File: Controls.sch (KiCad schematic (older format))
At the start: 2 parts

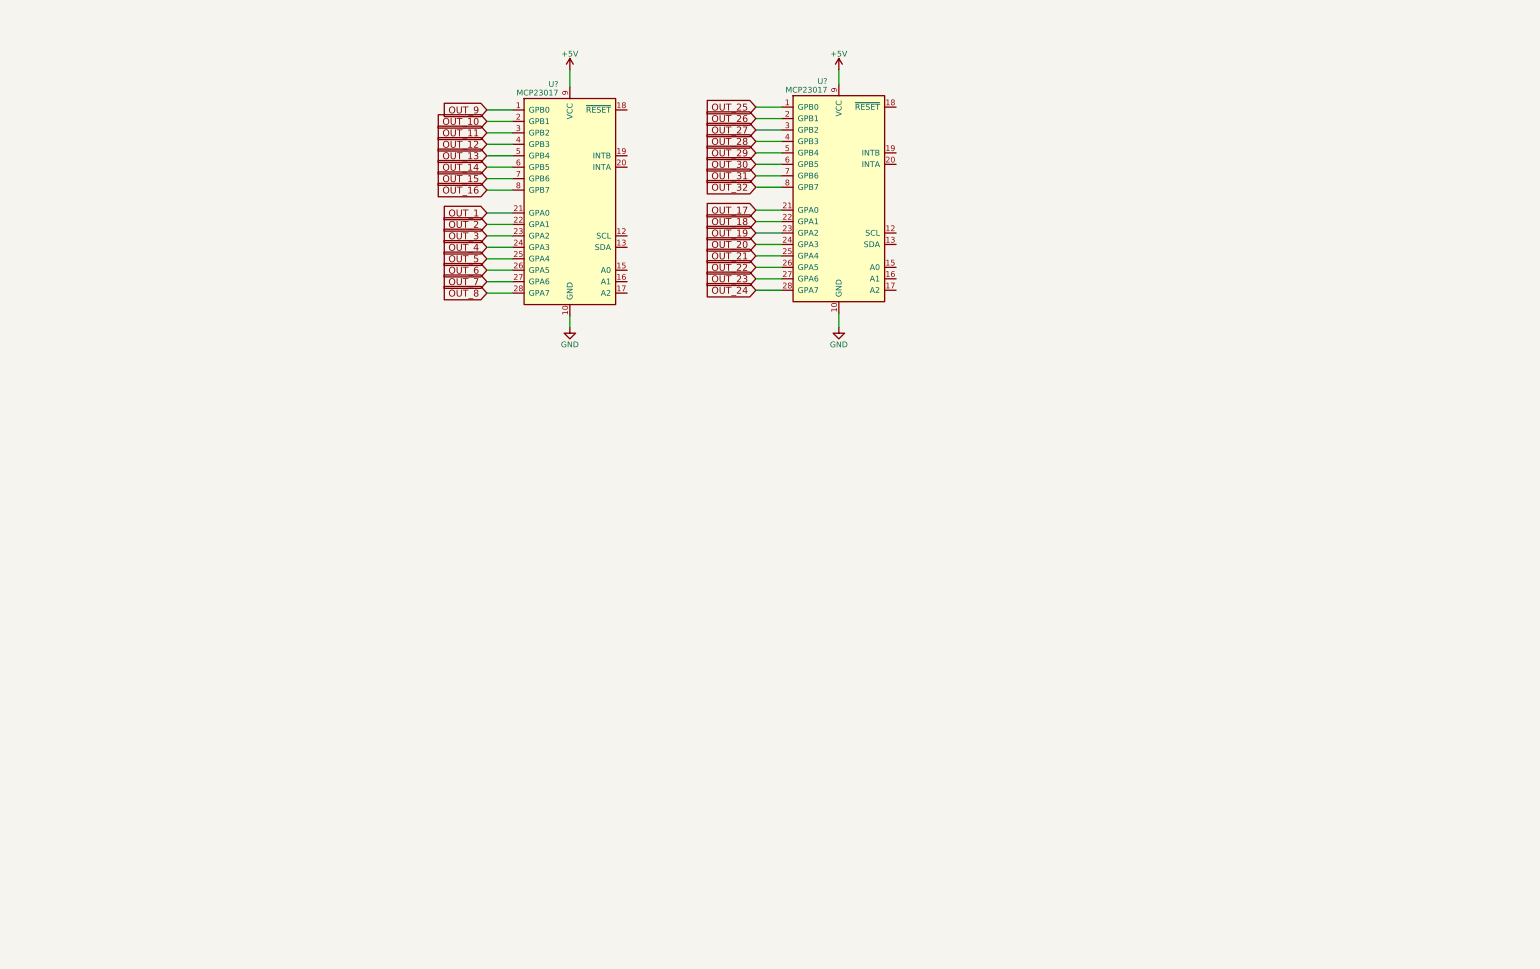
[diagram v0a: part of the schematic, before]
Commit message: Created arduino nano library for controls, no footprint yet. Created led-driver sheet for outputs from GPO to drive n-channel fets for low side driven control of led's
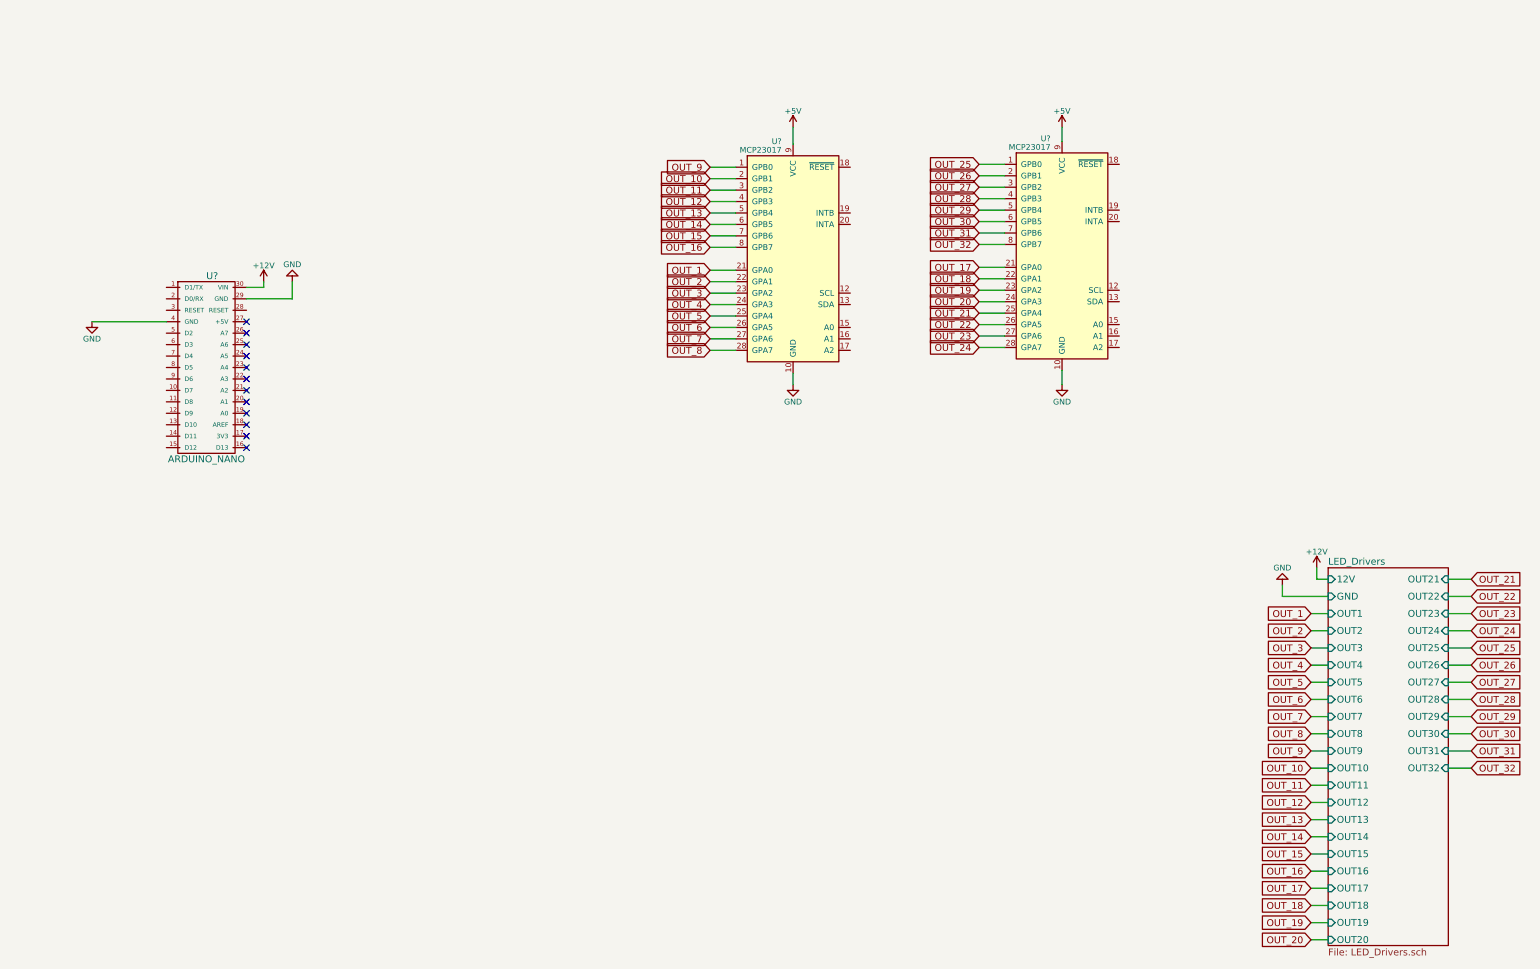
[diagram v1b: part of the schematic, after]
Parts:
- added U?: ARDUINO_NANO, symbol ARDUINO_NANO
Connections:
- net +12V: now also U?.30 (VIN)
- net GND: now also U?.29 (GND), U?.4 (GND)
- no-connect marks 0 -> 12
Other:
- moved on the sheet: U?

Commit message: Placed i2c labels and pull ups. Added 4 user input switches and MCP7940N RTC. Need to calculate capactiance for oscillator.
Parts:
- removed U? (x2): MCP23017, symbol MCP23017
- added BT?: Battery_Cell, symbol Battery_Cell
- added C? (x2): C, symbol C
- added R? (x7): 4.7K, symbol R
- added R?: 10K, symbol R
- added SW? (x4): SW_Push, symbol SW_Push
- added U? (x2): MCP23017, symbol MCP23017
- added U?: MCP7940N, symbol MCP7940N
- added Y?: Crystal, symbol Crystal
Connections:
- net labels added: MFP, SCL, SDA
- wire segments 83 -> 167
- no-connect marks 12 -> 23
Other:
- moved on the sheet: U?

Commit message: Started assigning footprints. Much cheaper to use the two channel n-fet for led driving. Need to change schematic to reflec.
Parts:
- added SW5: SW_Push, Buttons_Switches_SMD:SW_SPST_B3S-1000, symbol SW_Push
- BT1: renamed from BT?; footprint (none) -> Battery_Holders:Keystone_3001_1x12mm-CoinCell
- C6, C7: renamed from C?; value C -> 25pF; footprint (none) -> Capacitors_SMD:C_0805_HandSoldering
- R10, R3, R4, R5, R6, R7, R8, R9: renamed from R?; footprint (none) -> Resistors_SMD:R_0603_HandSoldering
- SW1, SW2, SW3, SW4: renamed from SW?; footprint (none) -> Buttons_Switches_SMD:SW_SPST_B3S-1000
- U4: renamed from U?; footprint (none) -> SMD_Packages:SOIC-8-N
- U5, U6: renamed from U?; footprint (none) -> SMD_Packages:SOIC-28
- Y1: renamed from Y?; footprint (none) -> Crystals:Crystal_AT310_d3.0mm_l10.0mm_Horizontal_1EP_style2
- gave numbers to parts that had none: 1
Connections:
- wire segments 167 -> 171

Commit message: Finished component footprint assignments and began rough layout of components.
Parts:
- U3: footprint (none) -> arduino:arduino_mini
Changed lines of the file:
@@
 LIBS:contrib
 LIBS:valves
+LIBS:NUD3124
 LIBS:WordClock-cache
 EELAYER 25 0
@@
 F 0 "U3" H 4500 5900 60  0000 C CNN
 F 1 "ARDUINO_NANO" H 4450 4300 60  0000 C CNN
-F 2 "" H 3900 4300 60  0001 C CNN
+F 2 "arduino:arduino_mini" H 3900 4300 60  0001 C CNN
 F 3 "" H 3900 4300 60  0001 C CNN
 	1    3900 4300

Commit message: Continued with routing and board layout.
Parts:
- U3: footprint arduino:arduino_mini -> Modules:Arduino_Nano
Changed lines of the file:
@@
 F 0 "U3" H 4500 5900 60  0000 C CNN
 F 1 "ARDUINO_NANO" H 4450 4300 60  0000 C CNN
-F 2 "arduino:arduino_mini" H 3900 4300 60  0001 C CNN
+F 2 "Modules:Arduino_Nano" H 3900 4300 60  0001 C CNN
 F 3 "" H 3900 4300 60  0001 C CNN
 	1    3900 4300

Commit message: Started placing and routing new board with updated schematic. Requries RTC.
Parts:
- removed BT1: Battery_Cell, Battery_Holders:Keystone_3001_1x12mm-CoinCell, symbol Battery_Cell
- removed C6, C7: 25pF, Capacitors_SMD:C_0805_HandSoldering, symbol C
- removed R4, R5: 4.7K, Resistors_SMD:R_0603_HandSoldering, symbol R
- removed SW2, SW3, SW4, SW5: SW_Push, Buttons_Switches_SMD:SW_SPST_B3S-1000, symbol SW_Push
- removed U4: MCP7940N, SMD_Packages:SOIC-8-N, symbol MCP7940N
- removed Y1: Crystal, Crystals:Crystal_AT310_d3.0mm_l10.0mm_Horizontal_1EP_style2, symbol Crystal
- added C3: 100nF, Capacitors_SMD:C_0805_HandSoldering, symbol C
- added J2: Conn_01x04, Connectors_Phoenix:PhoenixContact_MC-GF_04x3.50mm_Angled_ThreadedFlange, symbol Conn_01x04
- added Q1, Q2, Q3, Q4, Q5: Q_NMOS_GSD, TO_SOT_Packages_SMD:SOT-23_Handsoldering, symbol Q_NMOS_GSD
- added R9: 10K, Resistors_SMD:R_0603_HandSoldering, symbol R
- added U3: E2C-12NU, CustomFootprint:EC2-12NU, symbol E2C-12NU
- R3, R6, R7: value 4.7K -> 10K
- renumbered R9 to R4, R10 to R5, U3 to U2, U5 to U4, U6 to U5
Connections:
- net labels added: ButtonRead, LED_PWR, PWM_1_CTRL, PWM_1_OUTPUT, PWM_2_CTRL, PWM_2_OUTPUT, PWM_3_CTRL, PWM_3_OUTPUT, PWM_4_CTRL, PWM_4_OUTPUT, RelayControl
- net labels removed: 12V, 5V, MFP
- wire segments 171 -> 152
- no-connect marks 23 -> 27
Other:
- note removed: "SHARED POWER"
- moved on the sheet: R3, R4, R5, SW1, U2, U4, U5

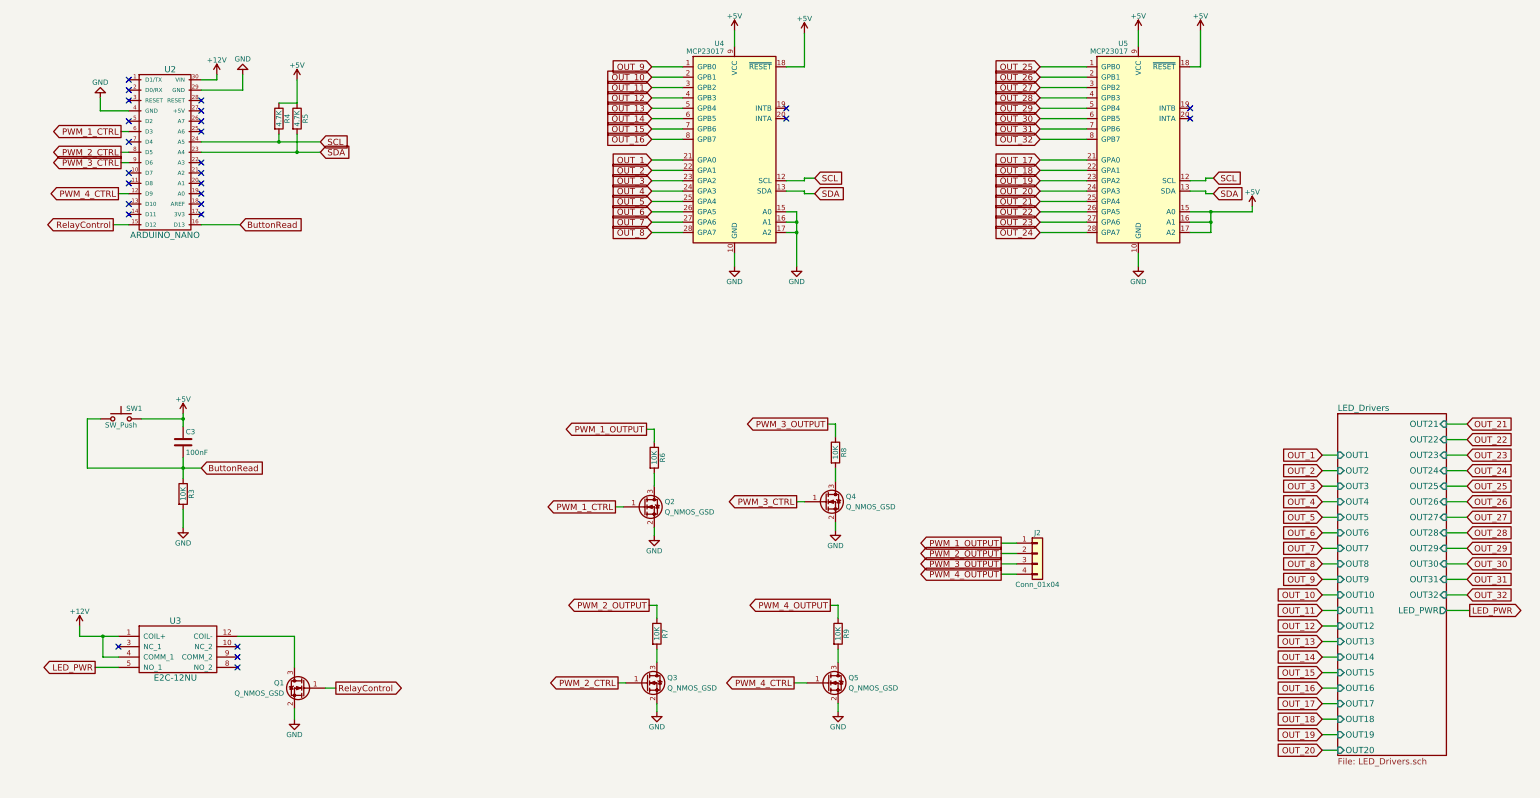
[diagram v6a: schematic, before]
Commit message: Fabriation files from first board spin. Footpring for IO expander incorrect, wide version used now, began board routing with new footprints.
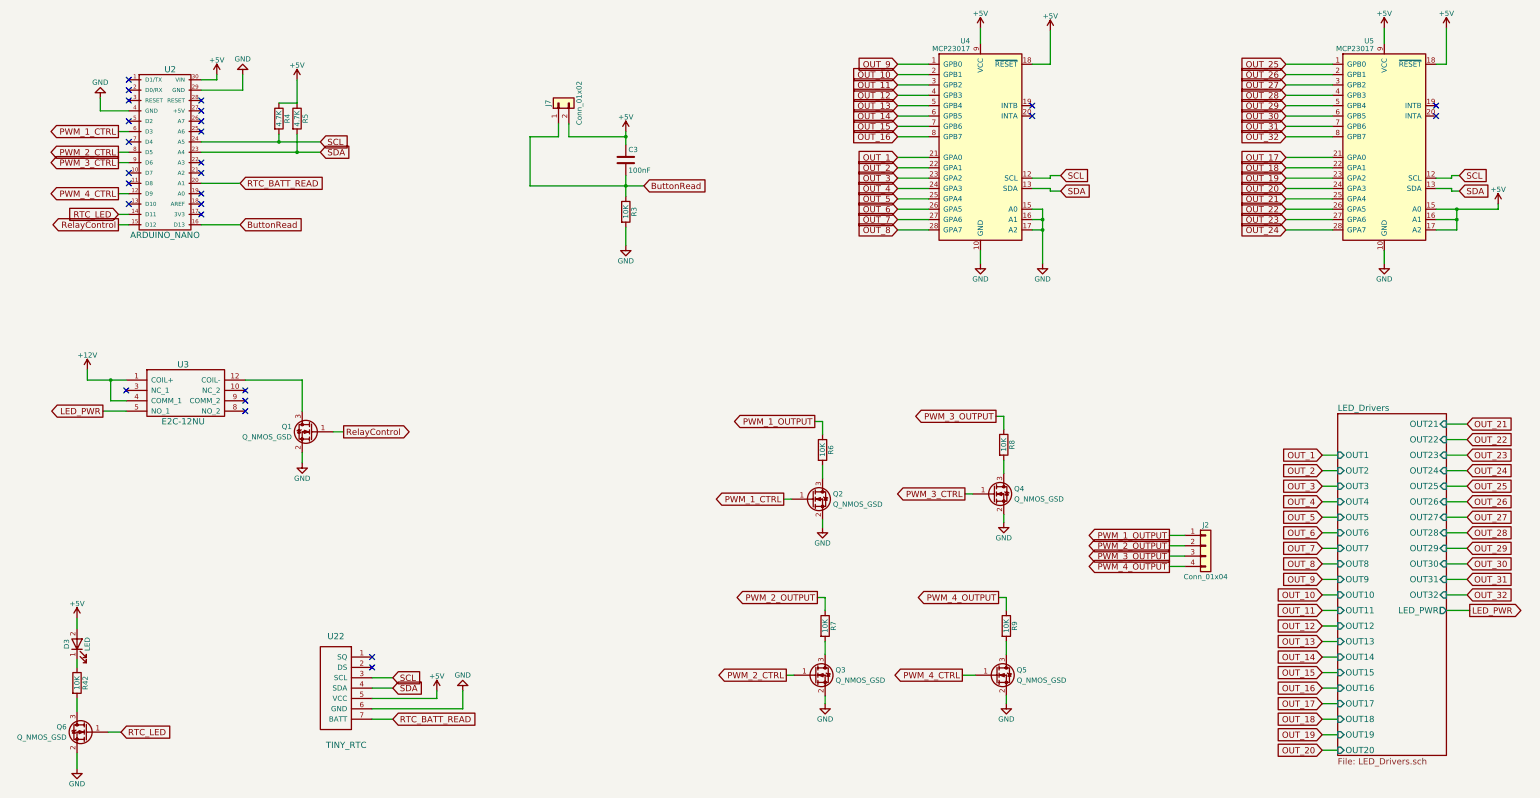
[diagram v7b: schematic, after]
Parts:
- removed SW1: SW_Push, Buttons_Switches_SMD:SW_SPST_B3S-1000, symbol SW_Push
- added D3: LED, LEDs:LED_0805_HandSoldering, symbol LED
- added J7: Conn_01x02, Connectors_Phoenix:PhoenixContact_MC-G_02x3.50mm_Angled, symbol Conn_01x02
- added Q6: Q_NMOS_GSD, TO_SOT_Packages_SMD:SOT-23_Handsoldering, symbol Q_NMOS_GSD
- added R42: 10K, Resistors_SMD:R_0603_HandSoldering, symbol R
- added U22: TINY_RTC, CustomFootprint:tiny_rtc, symbol TINY_RTC
- J2: footprint Connectors_Phoenix:PhoenixContact_MC-GF_04x3.50mm_Angled_ThreadedFlange -> Connectors_Phoenix:PhoenixContact_MC-G_04x3.50mm_Angled
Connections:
- net +12V: no longer U2.30 (VIN)
- net +5V: now also U2.30 (VIN), D3.2 (A), J7.2 (Pin_2), U22.5 (VCC)
- net ButtonRead: now also J7.1 (Pin_1)
- net GND: now also Q6.2 (S), U22.6 (GND)
- net SCL: now also U22.3 (SCL)
- net SDA: now also U22.4 (SDA)
- net RTC_LED: now reaches U2.14 (D11)
- net RTC_LED: now also Q6.1 (G)
- net RTC_BATT_READ: now reaches U2.20 (A1)
- net RTC_BATT_READ: now also U22.7 (BATT)
- new net: Q6.3 (D), R42.2
- new net: D3.1 (K), R42.1
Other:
- moved on the sheet: C3, J2, Q1, Q2, Q3, Q4, Q5, R3, R6, R7, R8, R9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
